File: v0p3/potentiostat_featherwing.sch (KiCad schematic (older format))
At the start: 20 parts, among them J1 Screw_Terminal_01x03, J2 Conn_01x03, J3 Conn_01x02, U1 feather_wing, U2 TS5A3160, U3 MCP6004

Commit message: Remade pdf of schematic.
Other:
- note added: "Rodeostat FeatherWing V0.3 R1"
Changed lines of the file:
@@
 Wire Wire Line
 	8700 1800 8700 1900
+Text Notes 7175 6850 0    50   ~ 0
+Rodeostat FeatherWing V0.3 R1
 $EndSCHEMATC

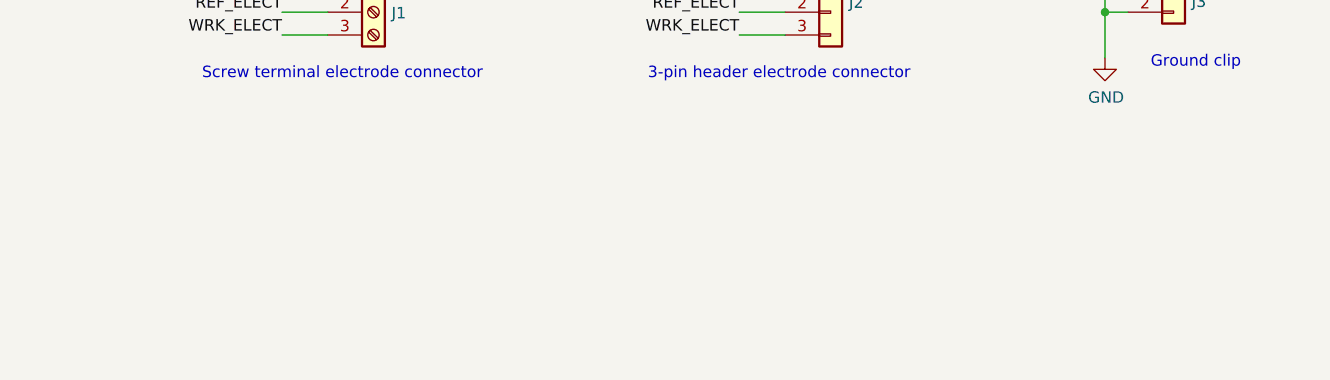
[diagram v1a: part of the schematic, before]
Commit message: Remade pdf of schematic add links to repositories.
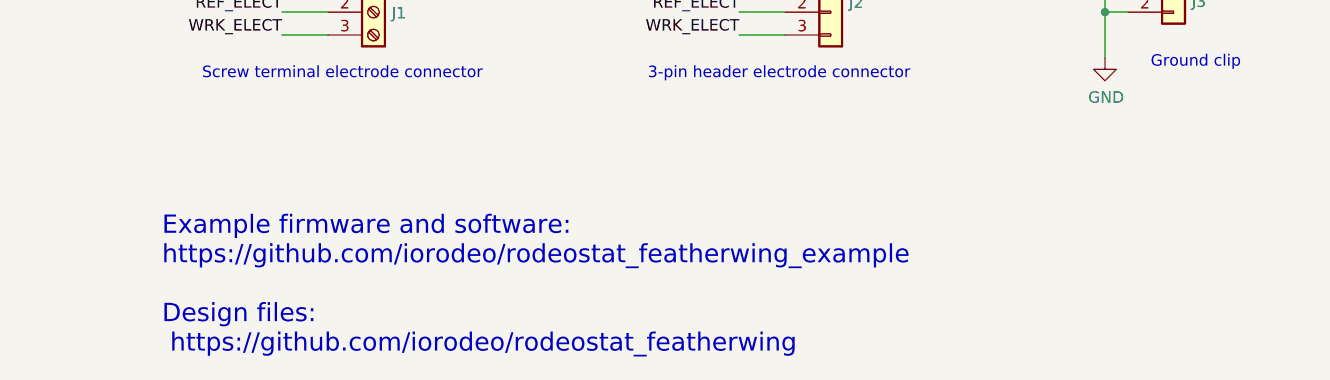
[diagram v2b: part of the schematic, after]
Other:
- note added: "Example firmware and software: \nhttps://github.com/iorodeo/rodeostat_featherwing_example\n\nDesign files:\n https://github.com/iorodeo/rodeostat_featherwing"
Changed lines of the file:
@@
 Text Notes 7175 6850 0    50   ~ 0
 Rodeostat FeatherWing V0.3 R1
+Text Notes 1325 7350 0    80   ~ 0
+Example firmware and software: \nhttps://github.com/iorodeo/rodeostat_featherwing_example\n\nDesign files:\n https://github.com/iorodeo/rodeostat_featherwing
 $EndSCHEMATC

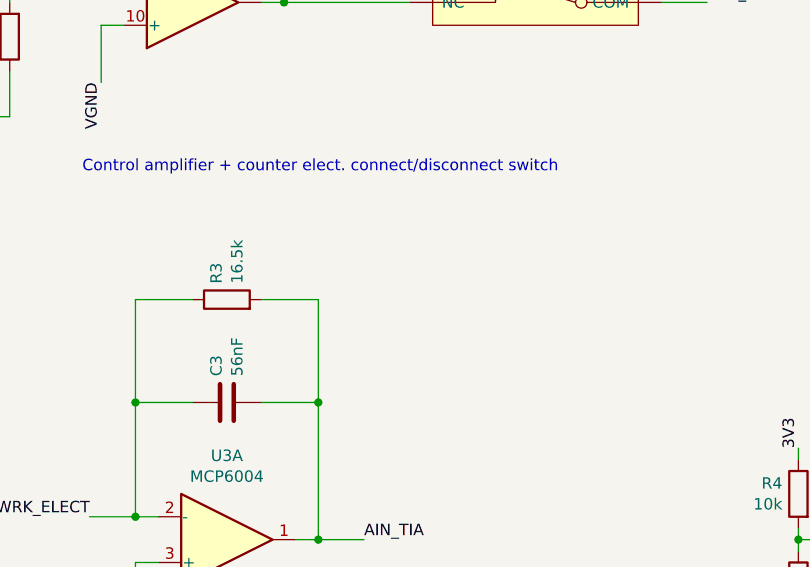
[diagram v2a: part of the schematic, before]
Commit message: Modified schematics so resistor values for different current ranges are shown.
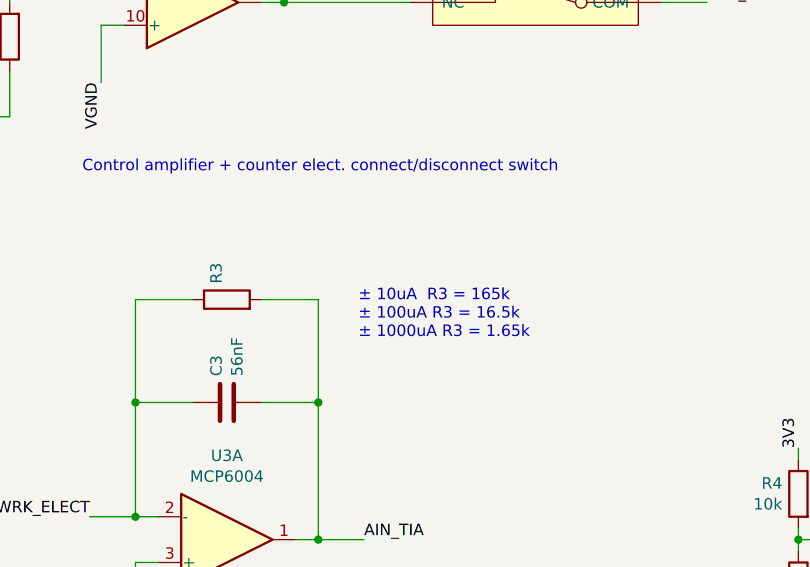
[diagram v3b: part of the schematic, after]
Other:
- note added: "± 10uA R3 = 165k\n± 100uA R3 = 16.5k\n± 1000uA R3 = 1.65k"
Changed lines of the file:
@@
 P 5800 3250
 F 0 "R3" H 5870 3296 50  0000 L CNN
-F 1 "16.5k" H 5870 3205 50  0000 L CNN
+F 1 "16.5k" H 5870 3205 50  0001 L CNN
 F 2 "Resistor_SMD:R_0603_1608Metric_Pad0.98x0.95mm_HandSolder" V 5730 3250 50  0001 C CNN
 F 3 "~" H 5800 3250 50  0001 C CNN
@@
 Text Notes 1325 7350 0    80   ~ 0
 Example firmware and software: \nhttps://github.com/iorodeo/rodeostat_featherwing_example\n\nDesign files:\n https://github.com/iorodeo/rodeostat_featherwing
+Text Notes 6375 3425 0    50   ~ 0
+± 10uA  R3 = 165k\n± 100uA R3 = 16.5k\n± 1000uA R3 = 1.65k
 $EndSCHEMATC
